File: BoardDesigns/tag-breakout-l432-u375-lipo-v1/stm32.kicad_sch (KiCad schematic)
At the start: 15 parts, among them J3 Conn_01x17, J4 Conn_01x17, Q1 Q_NPN_BEC, U11 TPS7A0218PDQNR, U3 stm32U375, U6 RV-3028-C7

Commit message: update design
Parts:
- Q1: symbol Device:Q_NPN_BEC -> Transistor_BJT:Q_NPN_BEC; MFN (none) -> Nexperia; MPN (none) -> BCX70H,215
- U3: symbol tag-library:stm32l432 -> libraries:stm32u375
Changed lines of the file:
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@@
 	)
 	(symbol
-		(lib_id "Device:Q_NPN_BEC")
+		(lib_id "Transistor_BJT:Q_NPN_BEC")
 		(at 138.43 162.56 0)
 		(unit 1)
@@
 			)
 		)
-		(property "Datasheet" ""
+		(property "Datasheet" "https://assets.nexperia.com/documents/data-sheet/BCX70H.pdf"
 			(at 138.43 162.56 0)
 			(hide yes)
@@
 			)
 		)
-		(property "Description" ""
-			(at 138.43 162.56 0)
-			(hide yes)
-			(show_name no)
-			(do_not_autoplace no)
-			(effects
-				(font
-					(size 1.27 1.27)
-				)
-			)
-		)
-		(property "JLCPCB" ""
+		(property "Description" "NPN transistor, base/emitter/collector"
 			(at 138.43 162.56 0)
 			(hide yes)
@@
 			)
 		)
-		(property "Digikey" ""
+		(property "MFN" "Nexperia"
+			(at 138.43 162.56 0)
+			(hide yes)
+			(show_name no)
+			(do_not_autoplace no)
+			(effects
+				(font
+					(size 1.27 1.27)
+				)
+			)
+		)
+		(property "MPN" "BCX70H,215"
+			(at 138.43 162.56 0)
+			(hide yes)
+			(show_name no)
+			(do_not_autoplace no)
+			(effects
+				(font
+					(size 1.27 1.27)
+				)
+			)
+		)
+		(property "Sim.Device" "NPN"
+			(at 138.43 162.56 0)
+			(hide yes)
+			(show_name no)
+			(do_not_autoplace no)
+			(effects
+				(font
+					(size 1.27 1.27)
+				)
+			)
+		)
+		(property "Sim.Pins" "1=B 2=E 3=C"
 			(at 138.43 162.56 0)
 			(hide yes)
@@
 	)
 	(symbol
-		(lib_id "tag-library:stm32l432")
+		(lib_id "libraries:stm32u375")
 		(at 40.64 72.39 0)
 		(unit 1)
@@
 			)
 		)
-		(property "Datasheet" ""
+		(property "Datasheet" "file:///Users/geobrown/Research/tag-designs/hardware/libraries/datasheets/stm32u375ce.pdf"
 			(at 40.64 72.39 0)
 			(hide yes)

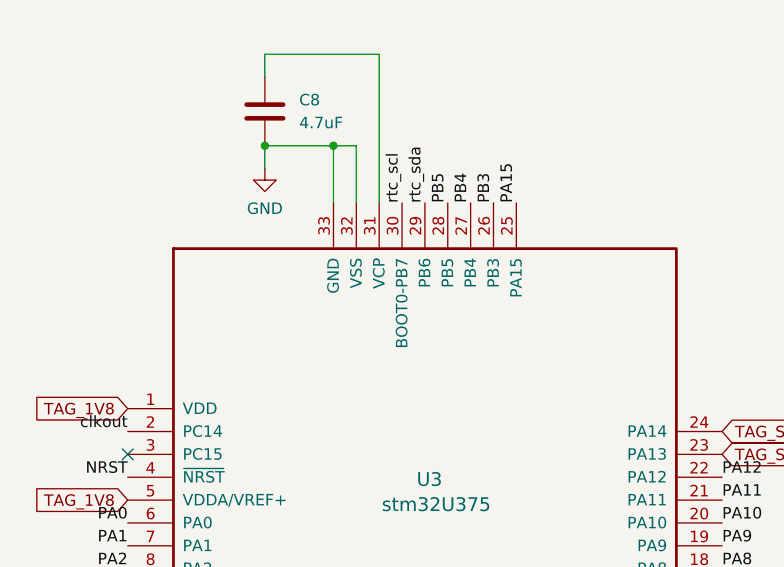
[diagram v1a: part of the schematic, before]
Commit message: check in 2 layer board
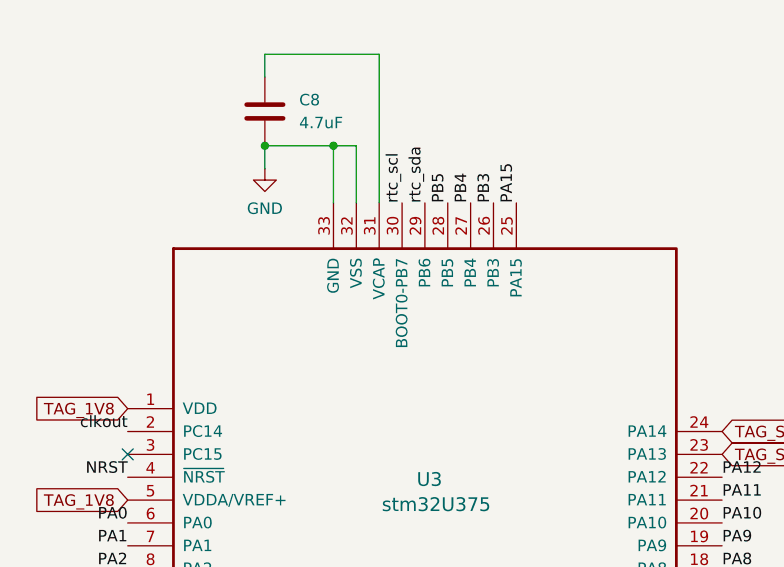
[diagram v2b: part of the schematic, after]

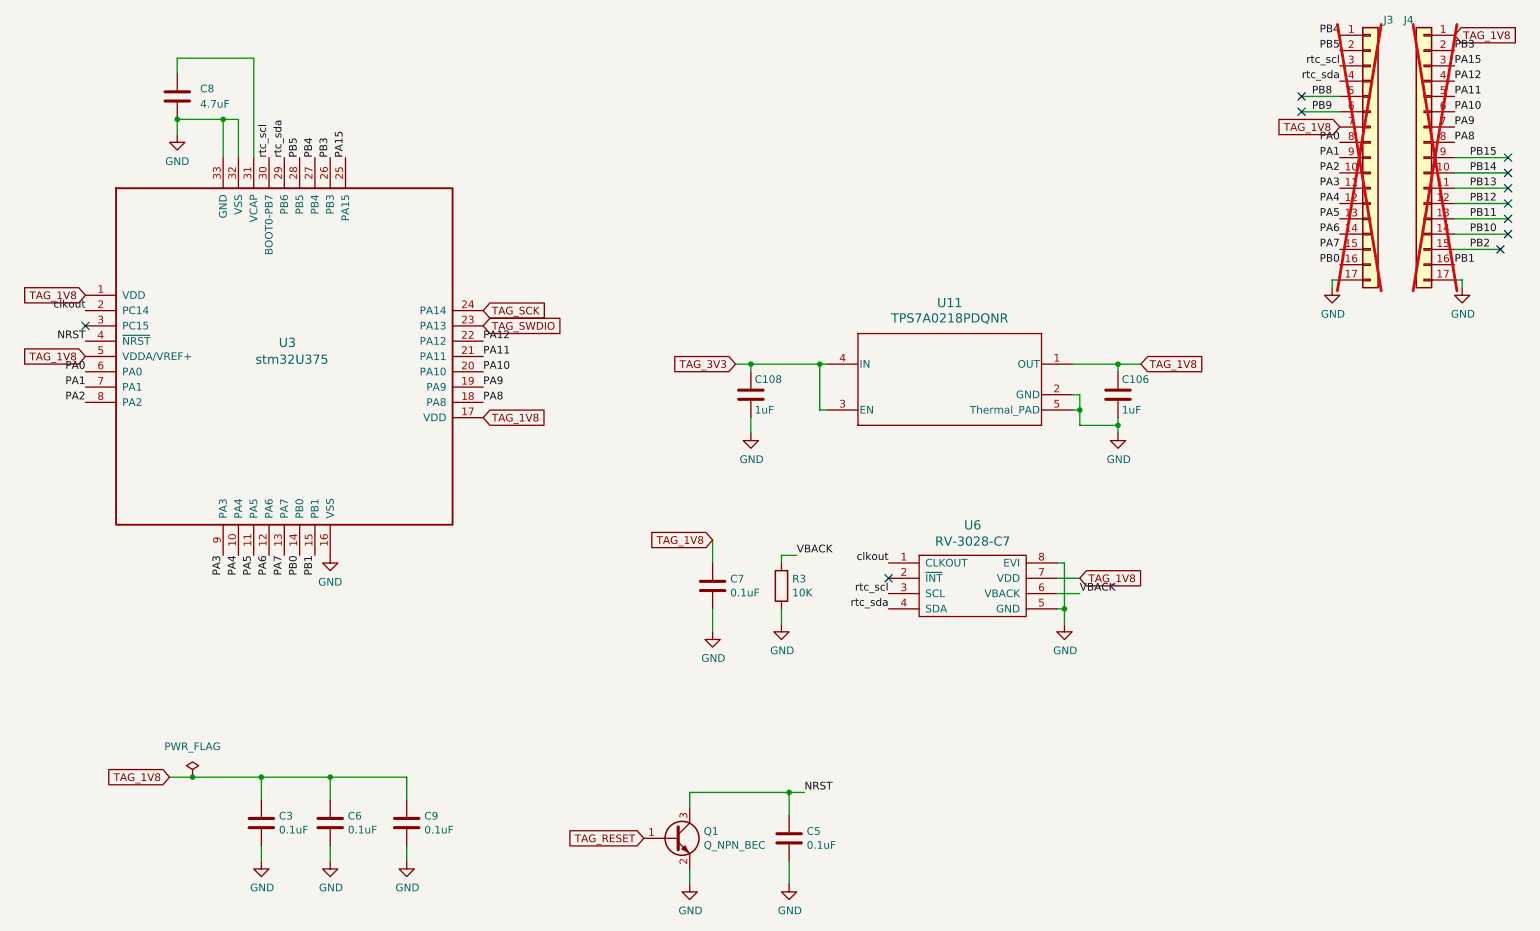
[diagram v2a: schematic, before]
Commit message: Update IMU breakout and bittag base designs
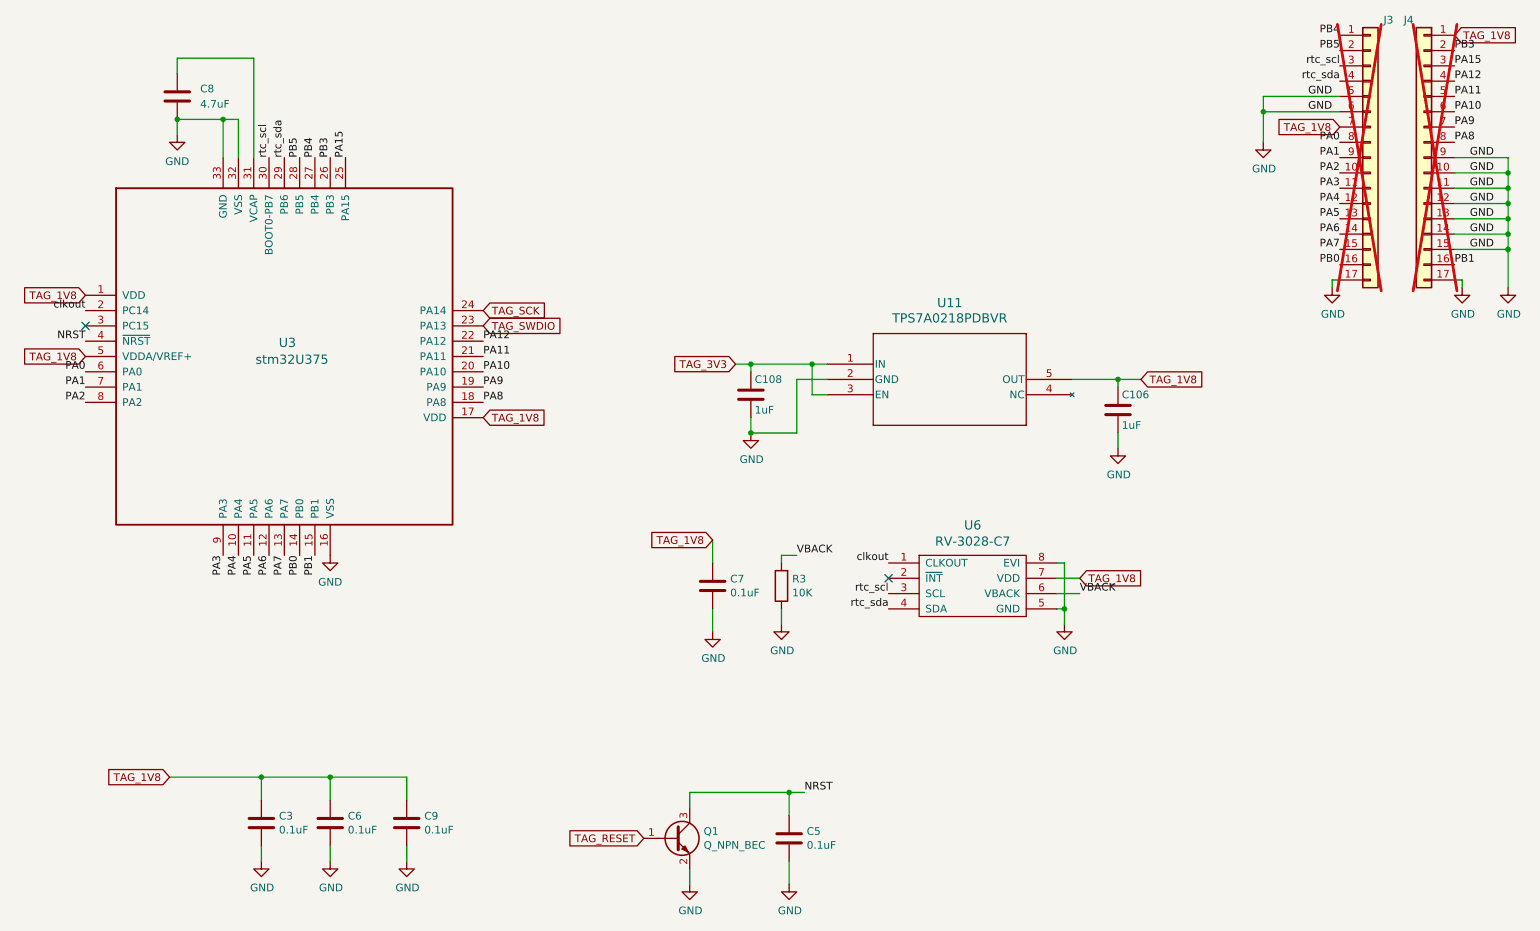
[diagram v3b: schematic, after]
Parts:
- removed U11: TPS7A0218PDQNR, Package_SON:Texas_X2SON-4_1x1mm_P0.65mm, symbol libraries:TPS7A0218PDQNR
- added U11: TPS7A0218PDBVR, Package_TO_SOT_SMD:SOT-23-5, symbol libraries:TPS7A0218PDBVR
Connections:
- net PB10 is gone; now on net GND: J4.14 (Pin_14)
- net PB11 is gone; now on net GND: J4.13 (Pin_13)
- net PB12 is gone; now on net GND: J4.12 (Pin_12)
- net PB13 is gone; now on net GND: J4.11 (Pin_11)
- net PB14 is gone; now on net GND: J4.10 (Pin_10)
- net PB15 is gone; now on net GND: J4.9 (Pin_9)
- net PB2 is gone; now on net GND: J4.15 (Pin_15)
- net PB8 is gone; now on net GND: J3.5 (Pin_5)
- net PB9 is gone; now on net GND: J3.6 (Pin_6)
- net GND: now also U11.2 (GND)
- net TAG_1V8: now also U11.5 (OUT)
- net TAG_3V3: now also U11.1 (IN), U11.3 (EN)
- no-connect marks 11 -> 2
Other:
- moved on the sheet: C106
